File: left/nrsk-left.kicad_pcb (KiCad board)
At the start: 2 copper layers, 157.1 x 133.5 mm, 125 parts, among them J1 USB-C, J2 USB-C, J3 OLED 128x32, SW1 Esc, SW10 2, SW11 3, SW12 4, SW13 5, SW14 6, SW15 Tab, SW16 Q, SW17 W, SW18 E, SW19 R, SW2 F1, SW20 T, SW21 Ctrl, SW22 A, SW23 S, SW24 D, SW25 F, SW26 G, SW27 Shift, SW28 Z, SW29 X, SW3 F2, SW30 C, SW31 V, SW32 B, SW33 Ctrl, SW34 Opt, SW35 Cmd, SW36 Space, SW37 Space, SW38 Space, SW4 F3, SW5 F4, SW6 F5, SW7 F6, SW8 `, SW9 1, U1 RP2040, U2 USBLC6-2SC6, U4 AP2112K-3.3, U5 W25Q128JVS, Y1 12MHz

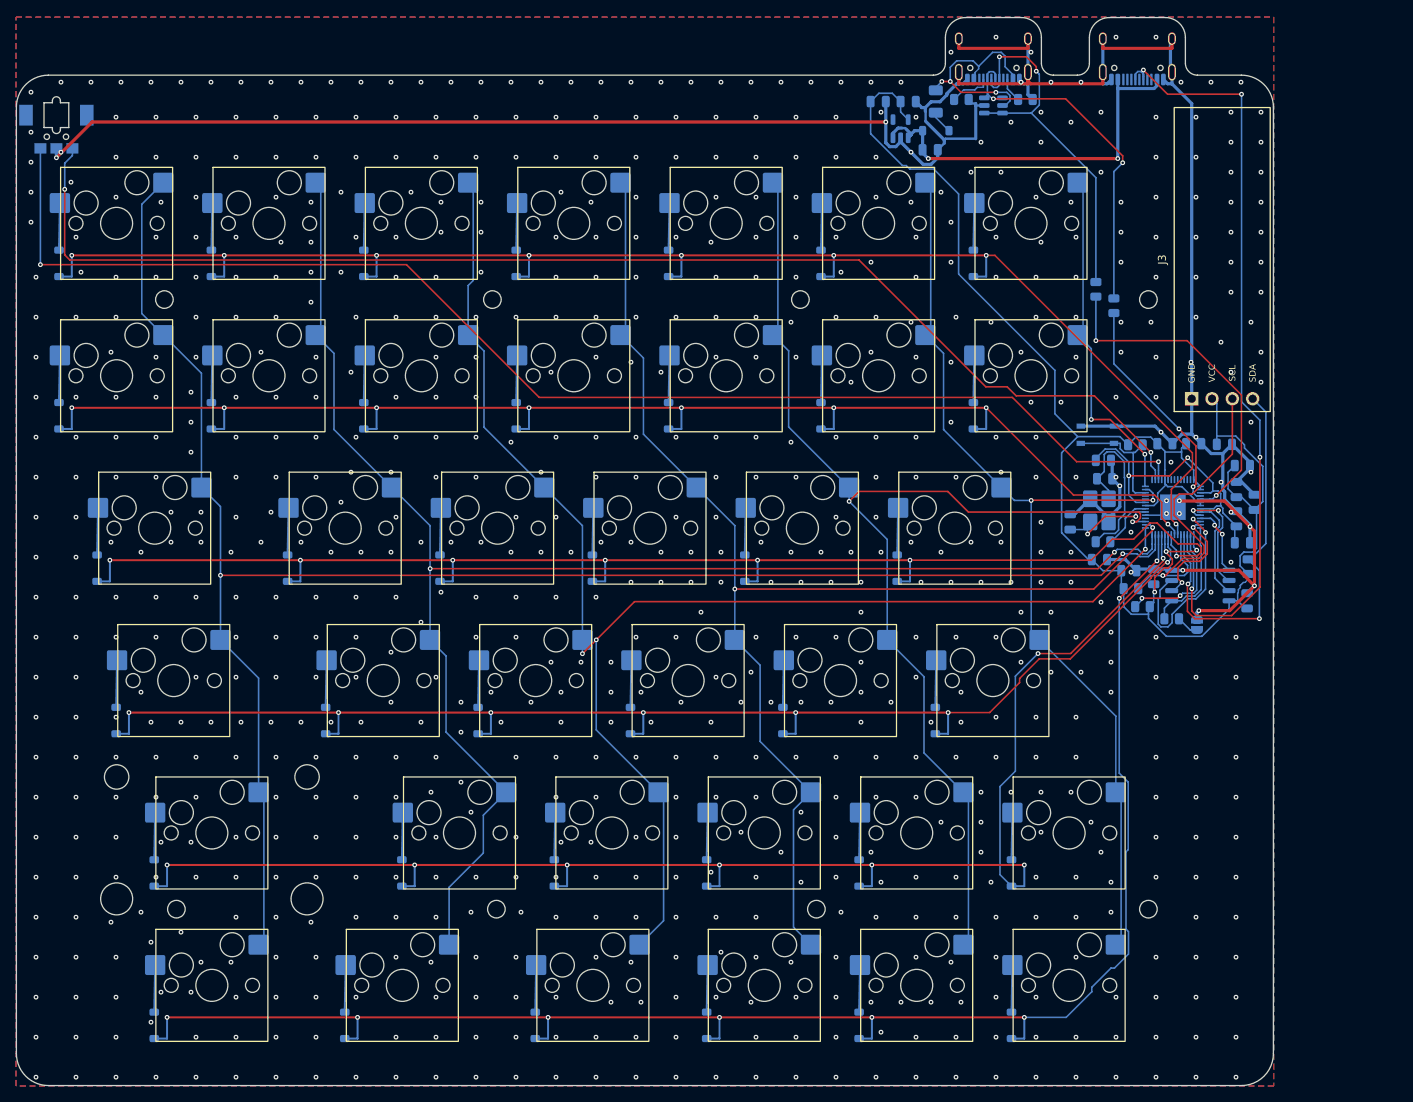
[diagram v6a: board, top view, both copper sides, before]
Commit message: OLED cover: 5.5 mm plate band, R7 on all four corners, display centred
The half-mirror cover now has the same R7 on all four corners. The corner facing the case corner stays
concentric with the case outline (R12.5 - band), so the band keeps its width round it; that sets the band to
5.5 mm (top, inner edge, row 0-1 keycaps), up from 3.5. The left board and case widen by 4 mm; the right
board keeps its size (its cover sits in the notch above the Y key).

The cover's bottom is no longer set by the row-2 keycap line: it runs 1.5 mm past the module's header end
(COVER_END), and the OLED sits where its display glass (3 mm toward the module's top) is the cover's centre
(OLED_Y 14.95). On the right the band down to the Y keycap is therefore 2.7 mm; make_case checks the band
beside the cover (5.5) and below it (COVER_BELOW, 2.5) separately. Perimeter screws within the band + 2 mm
of the cover go, so no screw head sits next to the rounded corner (10 case screws per side).

Sizes: boards 161.1 / 180.5 x 126.3 mm, cases 178.1 / 197.5 x 143.3 mm. README describes the cover; renders
and the A / B sheet are redone (1200 px).

Checked: ./build.sh -> left 0 unconnected (one 1.2 mm DATA stub and 47 zero-length router stubs removed),
right 0 unconnected, 0 parity issues, ERC 0 / 0, DRC 4 silkscreen-at-board-edge warnings per side as on
main; make_case.py checks ok on both halves (band, drum dial); make_jlc left 77 / right 81; textlint 0.

Co-Authored-By: Claude Opus 5.5 <noreply@anthropic.com>
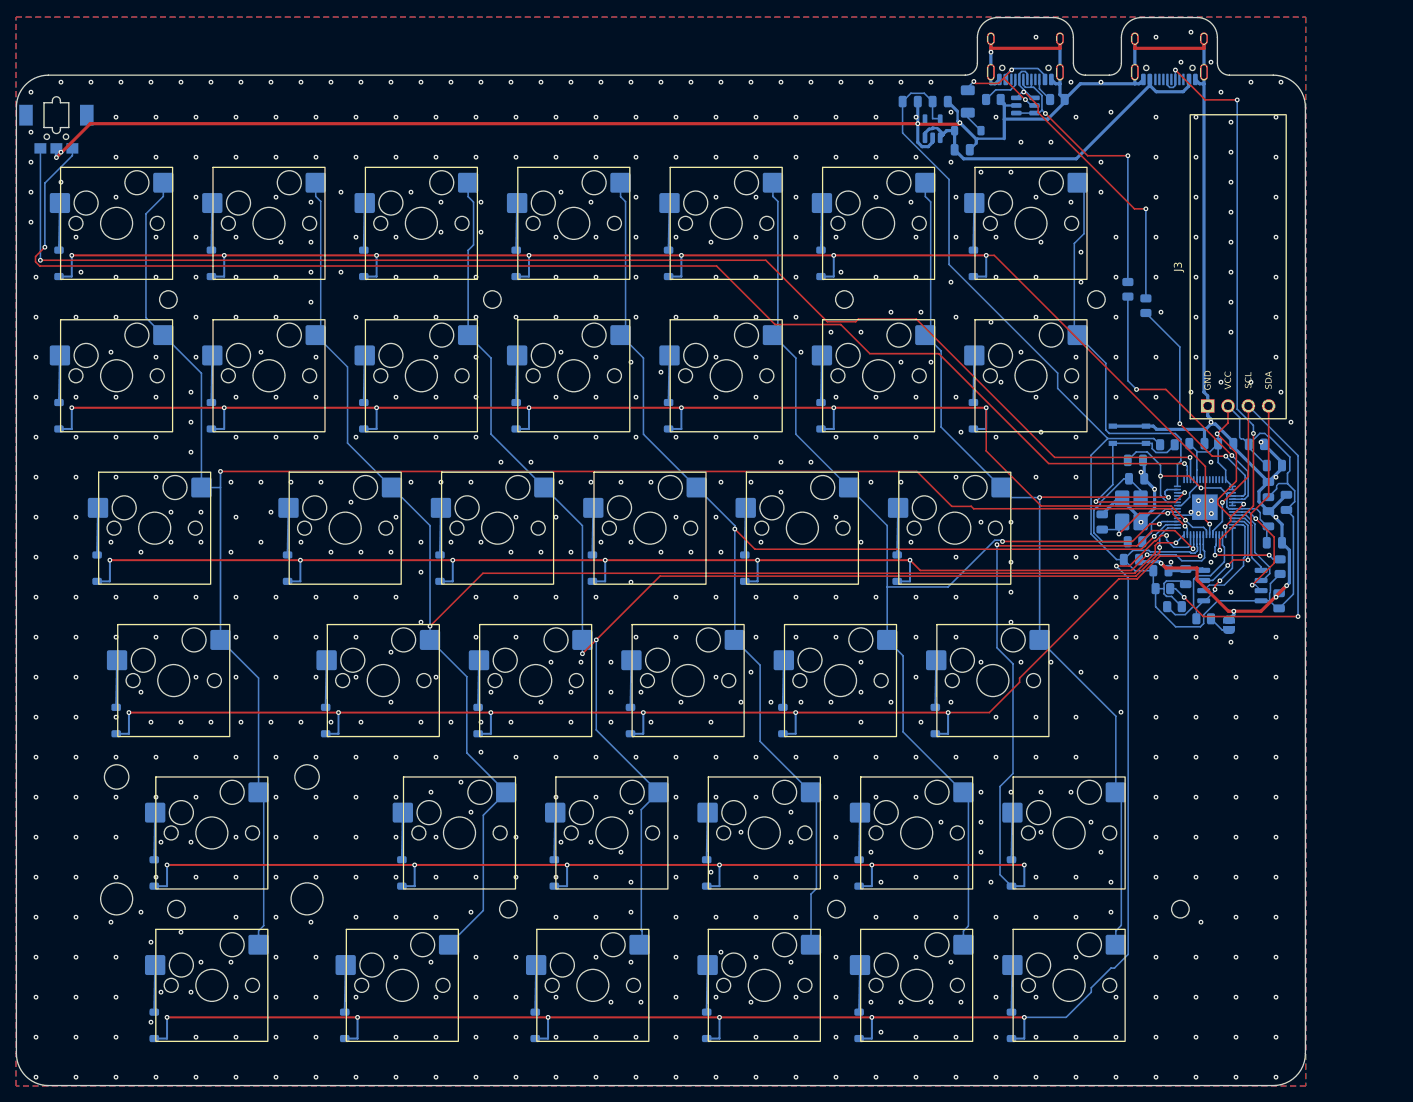
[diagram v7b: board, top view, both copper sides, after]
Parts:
- moved H4 6.50 mm to (162.0, 49.0)
- moved H3 5.50 mm to (130.5, 49.0)
- moved C1 4.00 mm to (162.7, 76.8)
- moved C11 4.00 mm to (166.4, 81.5)
- moved C12 4.00 mm to (174.6, 67.1)
- moved C13 4.00 mm to (178.2, 67.1)
- moved C14 4.00 mm to (184.2, 69.8)
- moved C15 4.00 mm to (185.8, 74.4)
- moved C16 4.00 mm to (145.2, 30.3)
- moved C17 4.00 mm to (142.5, 24.3)
- moved C18 4.00 mm to (182.0, 67.2)
- moved C19 4.00 mm to (138.7, 24.3)
- moved C2 4.00 mm to (167.0, 71.5)
- moved C20 4.00 mm to (184.8, 86.7)
- moved C3 4.00 mm to (183.5, 72.8)
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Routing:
- net /DATA: track 99.7 -> 73.9 mm
- net /SCL: track 43.3 -> 64.2 mm, vias 1 -> 3
- net /SDA: track 49.3 -> 30.5 mm
- net /3V3: track 204.6 -> 222.3 mm
- net /ROW4: track 188.1 -> 205.5 mm
- net GND: track 376.3 -> 360.7 mm, vias 776 -> 791
- net /RUN: track 15.5 -> 29.7 mm, vias 0 -> 2
- net /QSPI_SD2: track 25.4 -> 13.1 mm
- net /VBUS: track 27.9 -> 18.9 mm
- net /ENC_A: track 163.4 -> 172.3 mm
- net /USB_D+: track 47.3 -> 38.6 mm
- net /COL0: track 223.3 -> 230.7 mm
- net /D+: track 42.5 -> 35.4 mm
- net /ROW5: track 204.5 -> 211.6 mm
- net /1V1: track 38.4 -> 31.8 mm
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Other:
- board size 157.1 x 133.5 mm -> 161.1 x 133.5 mm

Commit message: Move the RP2040 and its support parts to the front, visible through the clear plate
- RP2040, flash, crystal, LDO, decoupling caps and resistors on the front, in the
  key-free strip along the inner edge (clear of every keycap and the OLED cover);
  USB-C and its protection parts, reset switch and BOOTSEL pad stay on the back
- RP2040 fixed with pin 1 top-left so its Raspberry Pi logo reads upright
  (datasheet Figure 168); make_pcb asserts the orientation
- Left half: pin row 1-14 faces the keys, so it is fanned out to 1 mm pitch and
  the matrix rows are routed by make_pcb; Freerouting does the rest
- build.sh retries routing until 0 unconnected and 0 DRC violations
- USB-C footprint copy in lib/nrsk.pretty with its outline on Fab (no clipped silk)
- JLC CPL handles top-side parts; front assembly drawing added
- Printed plate B: web cut away over the front-side parts
- DRC (all severities) 0, unconnected 0, parity 0, ERC 0 on both halves
- Docs, renders, fab outputs and case files regenerated

Co-Authored-By: Claude Opus 5.5 <noreply@anthropic.com>
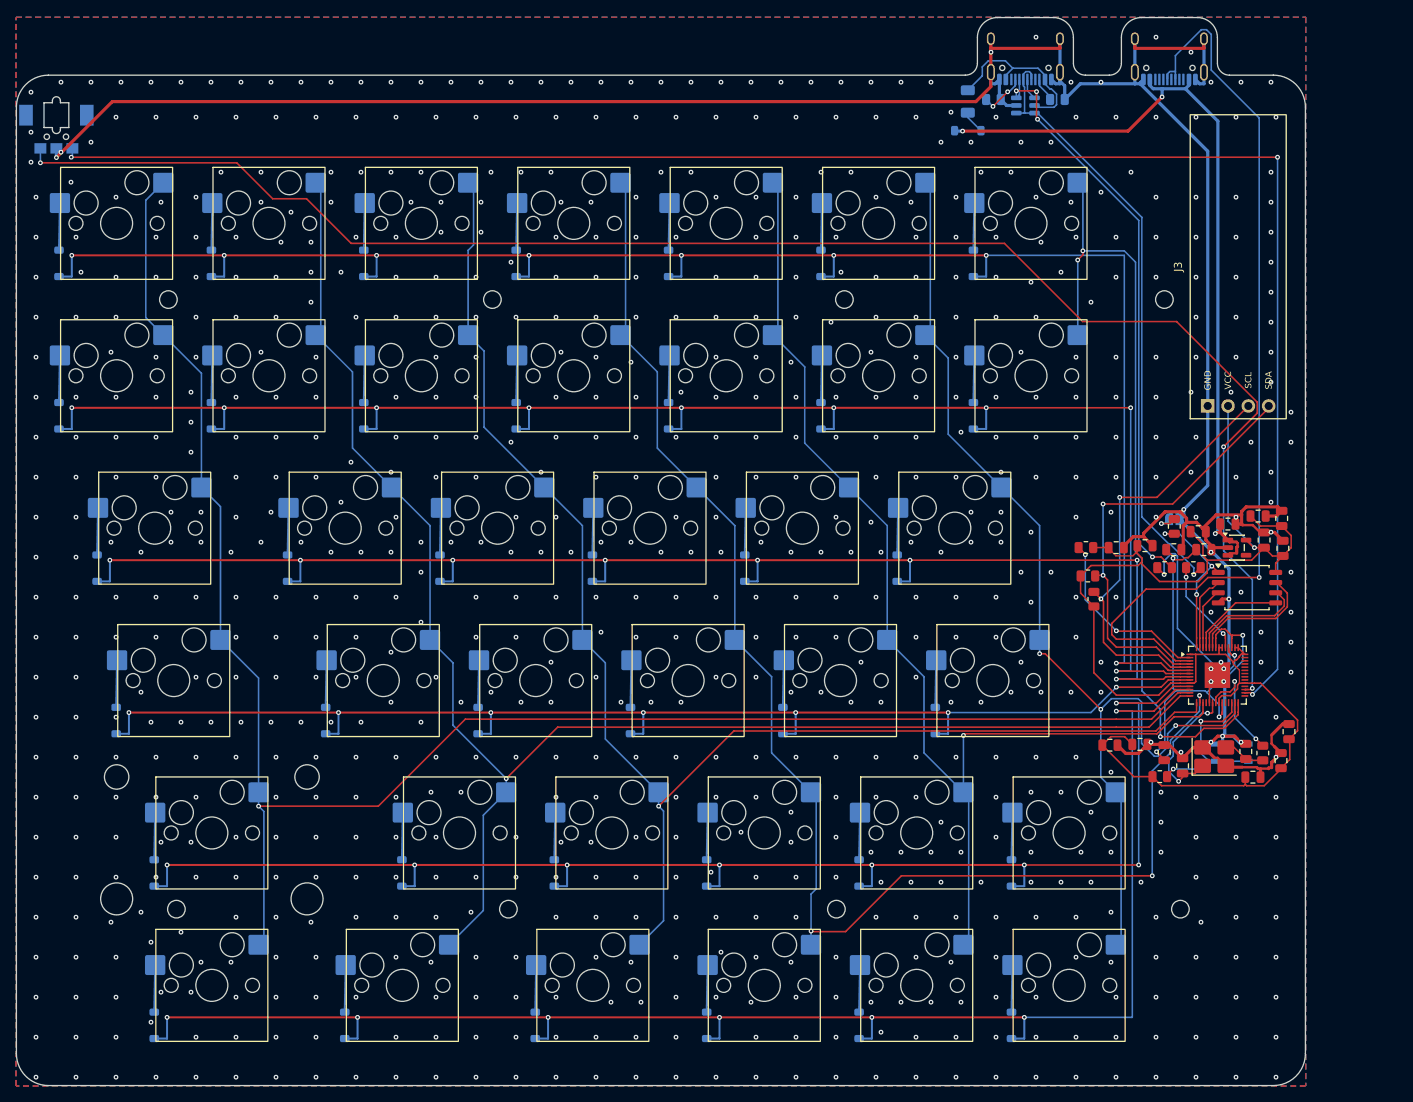
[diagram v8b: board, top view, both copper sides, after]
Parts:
- C1, C11, C12, C13, C14, C15, C16, C17, C18, C19, C2, C20, C3, C4, C5, C6, C7, C8, R1, R10, R2, R3, R6, R7, R8, R9, U1, U4, U5, Y1: moved to F.Cu
- J1, J2: footprint Connector_USB:USB_C_Receptacle_HRO_TYPE-C-31-M-12 -> nrsk:USB_C_Receptacle_HRO_TYPE-C-31-M-12
- moved C17 68.1 mm to (183.0, 79.1), turned to 90 degrees
- moved C19 67.6 mm to (182.2, 76.1)
- moved U4 64.7 mm to (179.6, 80.1), turned to 0 degrees
- moved C16 57.4 mm to (178.4, 77.1)
- moved C12 42.3 mm to (181.6, 108.8)
- moved RSW1 41.7 mm to (178.9, 105.7)
- moved R6 41.5 mm to (169.9, 108.7)
- moved C2 36.7 mm to (180.7, 105.5), turned to 90 degrees
- moved C5 36.7 mm to (170.5, 105.7), turned to 90 degrees
- moved R2 35.7 mm to (174.1, 82.6), turned to 0 degrees
- moved R3 32.8 mm to (170.5, 82.6), turned to 0 degrees
- moved Y1 32.5 mm to (176.7, 106.2), turned to 0 degrees
- moved C1 32.1 mm to (172.8, 107.3)
- moved C11 31.3 mm to (185.1, 106.7), turned to 90 degrees
- moved R10 30.9 mm to (182.8, 105.7), turned to 90 degrees
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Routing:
- net VCC: track 43.8 -> 99.9 mm, vias 0 -> 3
- net /3V3: track 222.3 -> 171.8 mm, vias 3 -> 1
- net /COL6: track 49.3 -> 99.7 mm, vias 0 -> 3
- net /ENC_A: track 172.3 -> 221.4 mm, vias 2 -> 3
- net /DATA: track 73.9 -> 114.6 mm, vias 4 -> 1
- net /USB_D+: track 38.6 -> 76.6 mm, vias 2 -> 1
- net /USB_D-: track 40.5 -> 76.6 mm, vias 2 -> 4
- net /ENC_B: track 171.0 -> 206.4 mm, vias 2 -> 3
- net /ROW0: track 191.1 -> 222.9 mm
- net /1V1: track 31.8 -> 57.9 mm, vias 2 -> 4
- net /ROW4: track 205.5 -> 180.1 mm
- net /SDA: track 30.5 -> 55.6 mm
- net /ROW1: track 181.6 -> 206.2 mm, vias 8 -> 9
- net /D+: track 35.4 -> 12.0 mm
- net GND: track 360.7 -> 375.9 mm, vias 791 -> 776
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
